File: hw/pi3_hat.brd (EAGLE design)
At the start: 56.5 x 65 mm, 119 parts, among them J1 XT30P, J2 XT30P, U1 AP64351SO8EP, U10 CAT24C32SOIC8, U11 STM32G474CEU6, U12 TCAN334GSOT23, U13 TCAN334GSOT23, U14 SPW2430HR5H-B, U2 DMMT5401, U3 DMG2305UX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

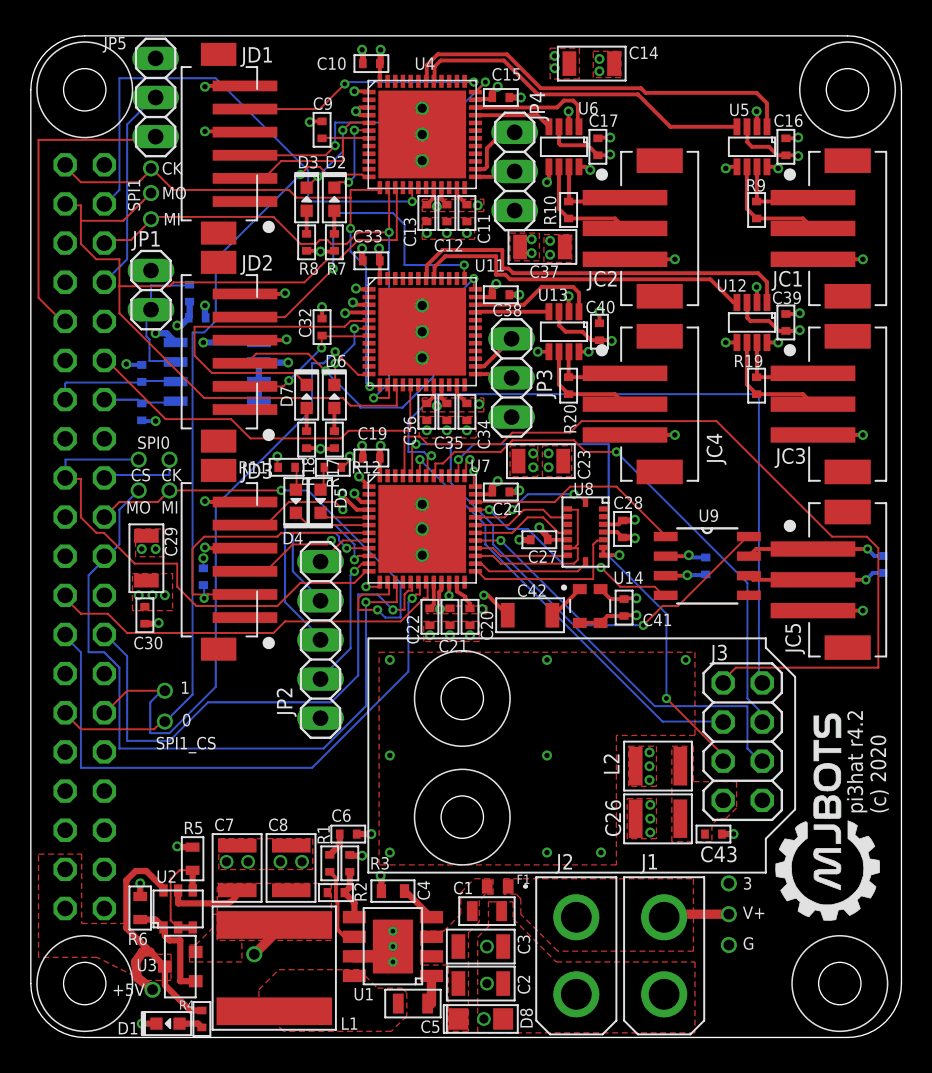
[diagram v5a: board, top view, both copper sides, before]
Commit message: Fine tweak silks
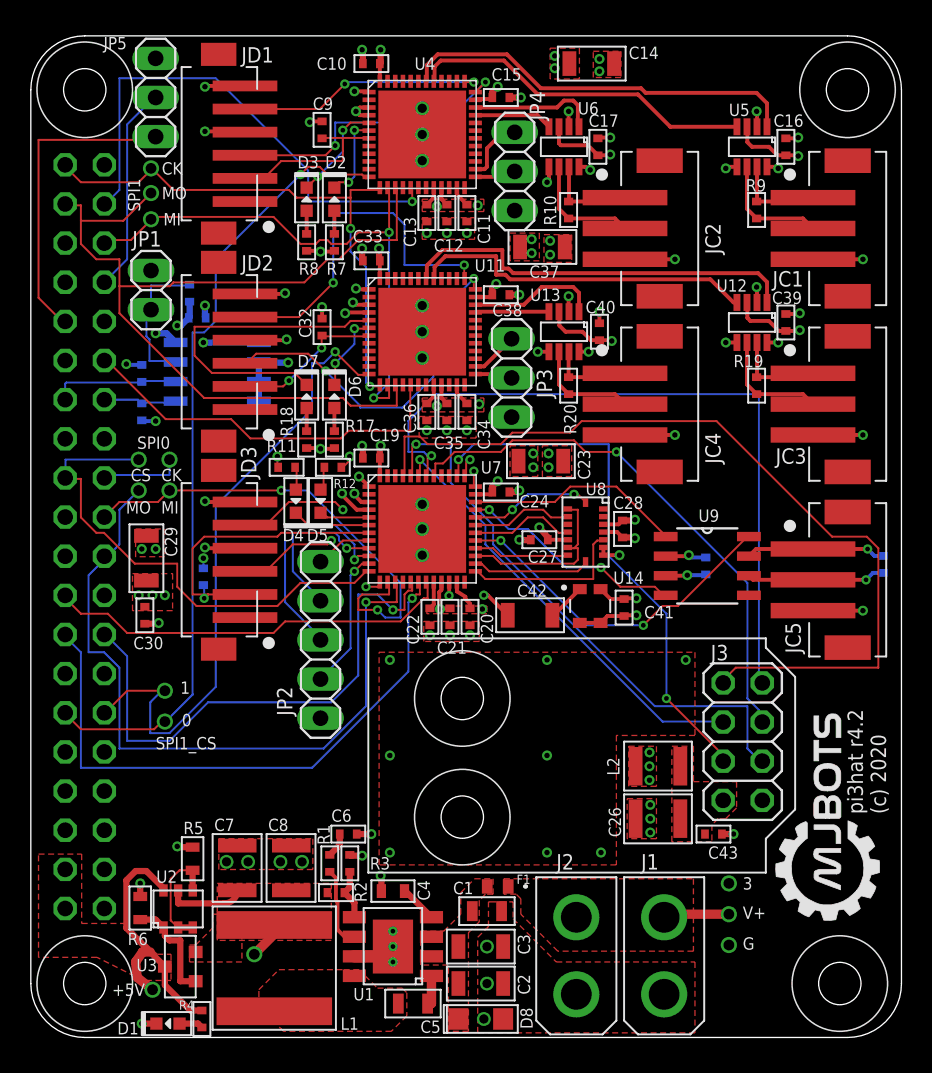
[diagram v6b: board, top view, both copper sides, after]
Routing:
- net N$34: track 23.0 -> 23.5 mm

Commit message: Update board rev to 4.1, since we haven't made one of those yet
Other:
- board text added: "pi3hat r4.1"
- board text removed: "pi3hat r4.2"
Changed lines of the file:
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@@
 <wire x1="53" y1="0" x2="56.5" y2="3.5" width="0" layer="20" curve="90"/>
 <text x="55.5" y="14.5" size="1" layer="21" font="vector" ratio="10" rot="R90">(c) 2020</text>
-<text x="54" y="14.5" size="1" layer="21" font="vector" ratio="10" rot="R90">pi3hat r4.2</text>
+<text x="54" y="14.5" size="1" layer="21" font="vector" ratio="10" rot="R90">pi3hat r4.1</text>
 <wire x1="21.95" y1="25.9" x2="47.7" y2="25.9" width="0.127" layer="21"/>
 <wire x1="47.7" y1="25.9" x2="47.7" y2="25.3" width="0.127" layer="21"/>
